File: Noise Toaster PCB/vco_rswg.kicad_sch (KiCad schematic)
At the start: 22 parts, among them Q1 NJFET, U1 LM324, U2 LM324

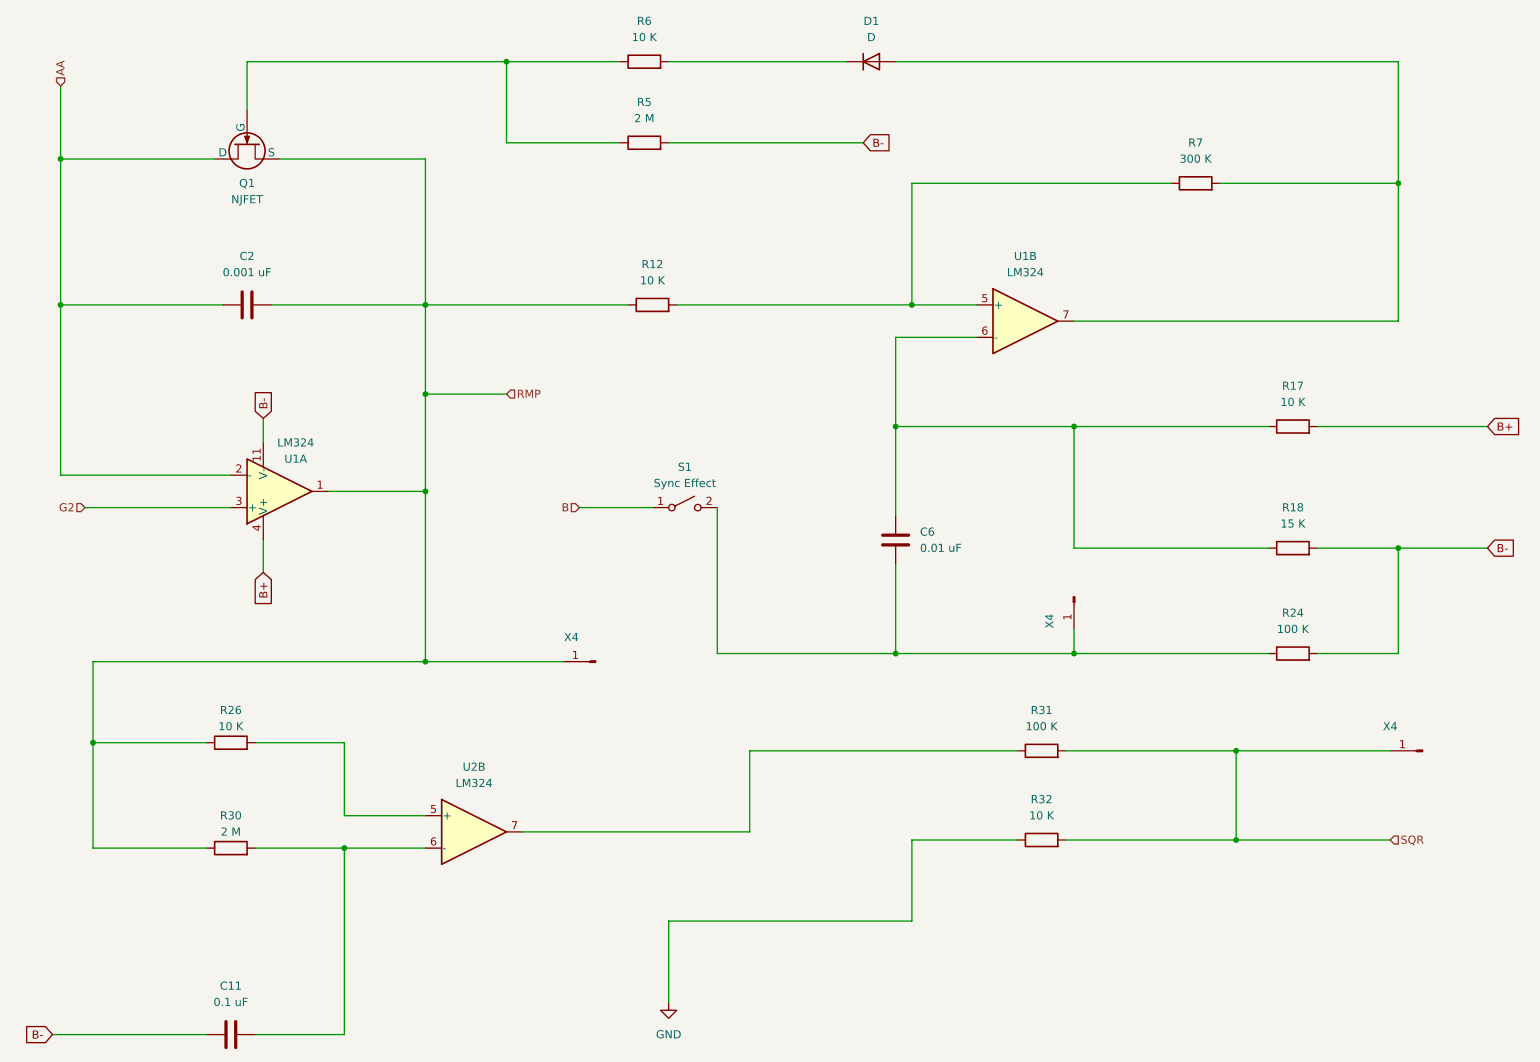
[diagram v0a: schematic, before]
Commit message: updated schematics
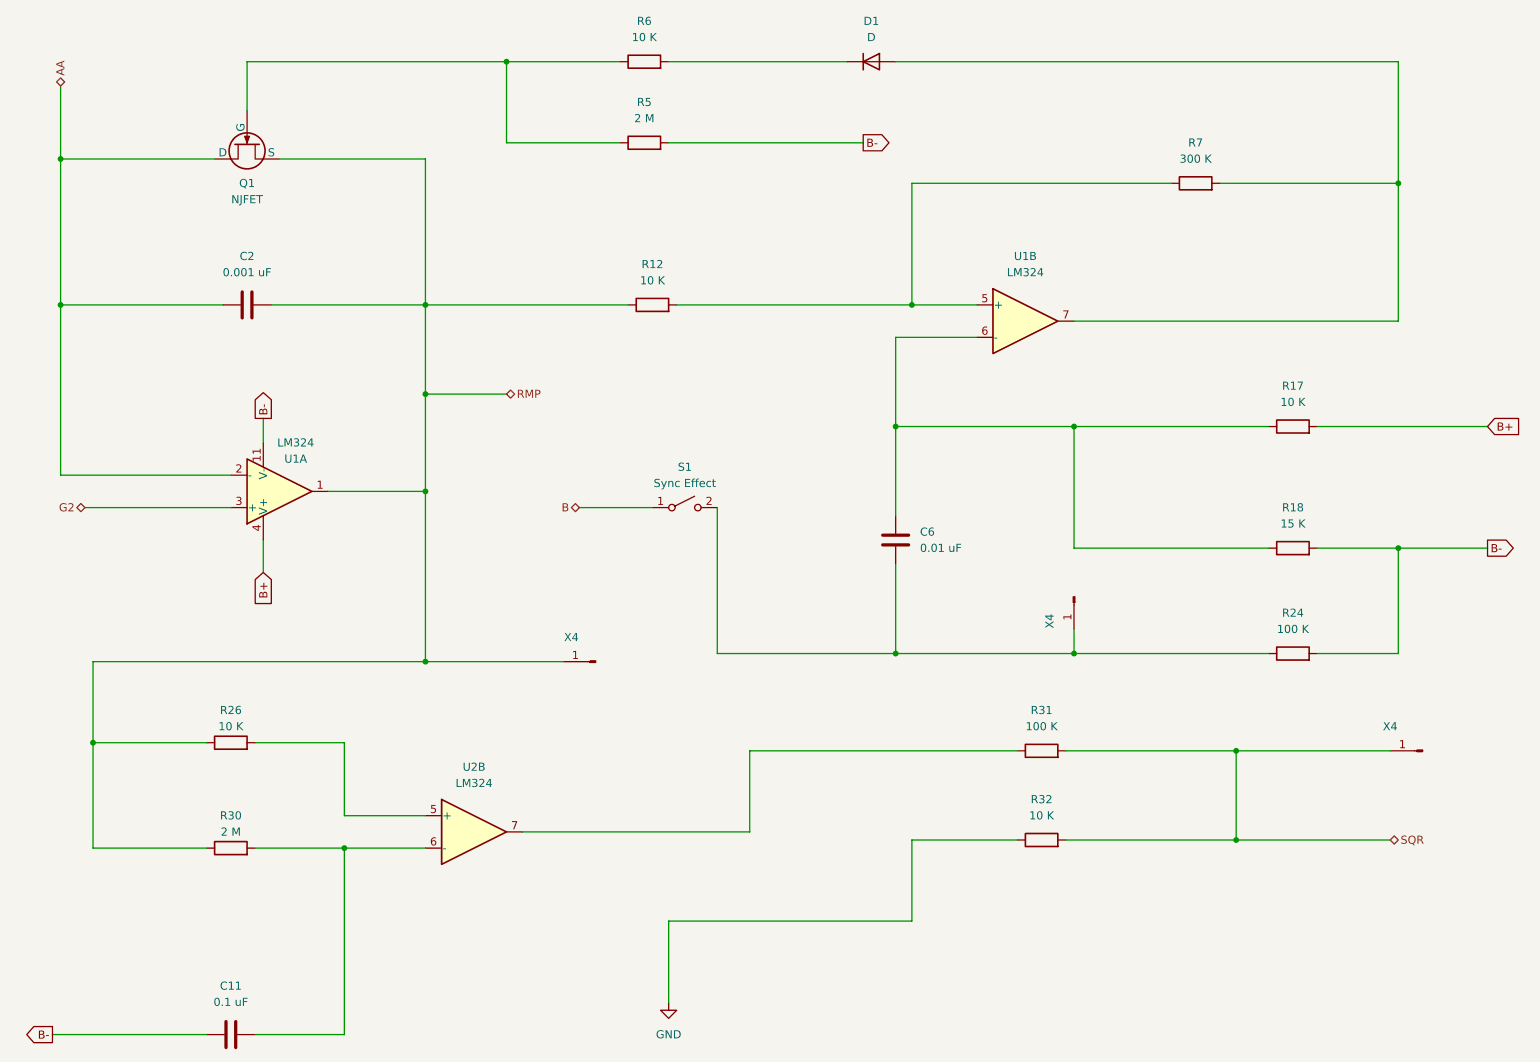
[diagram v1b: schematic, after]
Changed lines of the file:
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@@
     (stroke (width 0) (type default))
   )
-  (global_label "B-" (shape input) (at 157.48 38.1 0) (fields_autoplaced)
+  (global_label "B-" (shape output) (at 157.48 38.1 0) (fields_autoplaced)
     (effects (font (size 1.27 1.27)) (justify left))
     (property "Intersheetrefs" "${INTERSHEET_REFS}" (at 163.3076 38.1 0)
@@
     )
   )
-  (global_label "B-" (shape input) (at 30.48 177.8 180) (fields_autoplaced)
+  (global_label "B-" (shape output) (at 30.48 177.8 180) (fields_autoplaced)
     (effects (font (size 1.27 1.27)) (justify right))
     (property "Intersheetrefs" "${INTERSHEET_REFS}" (at 24.6524 177.8 0)
@@
     )
   )
-  (global_label "B-" (shape input) (at 63.5 81.28 90) (fields_autoplaced)
+  (global_label "B-" (shape output) (at 63.5 81.28 90) (fields_autoplaced)
     (effects (font (size 1.27 1.27)) (justify left))
     (property "Intersheetrefs" "${INTERSHEET_REFS}" (at 63.5 75.4524 90)
@@
     )
   )
-  (global_label "B-" (shape input) (at 255.27 101.6 0) (fields_autoplaced)
+  (global_label "B-" (shape output) (at 255.27 101.6 0) (fields_autoplaced)
     (effects (font (size 1.27 1.27)) (justify left))
     (property "Intersheetrefs" "${INTERSHEET_REFS}" (at 261.0976 101.6 0)
@@
     )
   )
-  (hierarchical_label "G2" (shape input) (at 35.56 95.25 180) (fields_autoplaced)
+  (hierarchical_label "G2" (shape bidirectional) (at 35.56 95.25 180) (fields_autoplaced)
     (effects (font (size 1.27 1.27)) (justify right))
   )
-  (hierarchical_label "B" (shape input) (at 113.03 95.25 180) (fields_autoplaced)
+  (hierarchical_label "B" (shape bidirectional) (at 113.03 95.25 180) (fields_autoplaced)
     (effects (font (size 1.27 1.27)) (justify right))
   )
-  (hierarchical_label "AA" (shape input) (at 31.75 29.21 90) (fields_autoplaced)
-    (effects (font (size 1.27 1.27)) (justify left))
-  )
-  (hierarchical_label "RMP" (shape input) (at 101.6 77.47 0) (fields_autoplaced)
-    (effects (font (size 1.27 1.27)) (justify left))
-  )
-  (hierarchical_label "SQR" (shape input) (at 240.03 147.32 0) (fields_autoplaced)
+  (hierarchical_label "AA" (shape bidirectional) (at 31.75 29.21 90) (fields_autoplaced)
+    (effects (font (size 1.27 1.27)) (justify left))
+  )
+  (hierarchical_label "RMP" (shape bidirectional) (at 101.6 77.47 0) (fields_autoplaced)
+    (effects (font (size 1.27 1.27)) (justify left))
+  )
+  (hierarchical_label "SQR" (shape bidirectional) (at 240.03 147.32 0) (fields_autoplaced)
     (effects (font (size 1.27 1.27)) (justify left))
   )
@@
     (instances
       (project "Noise Toaster PCB"
-        (path "/7be3f398-d902-4566-9ee4-0bff072cd47e/9c6b1f0b-dddb-43c5-83ba-4fcd1cf28662"
-          (reference "#PWR01") (unit 1)
-        )
         (path "/7be3f398-d902-4566-9ee4-0bff072cd47e/a3e9deee-1b9d-4545-a3c9-71b211642b5b"
           (reference "#PWR04") (unit 1)

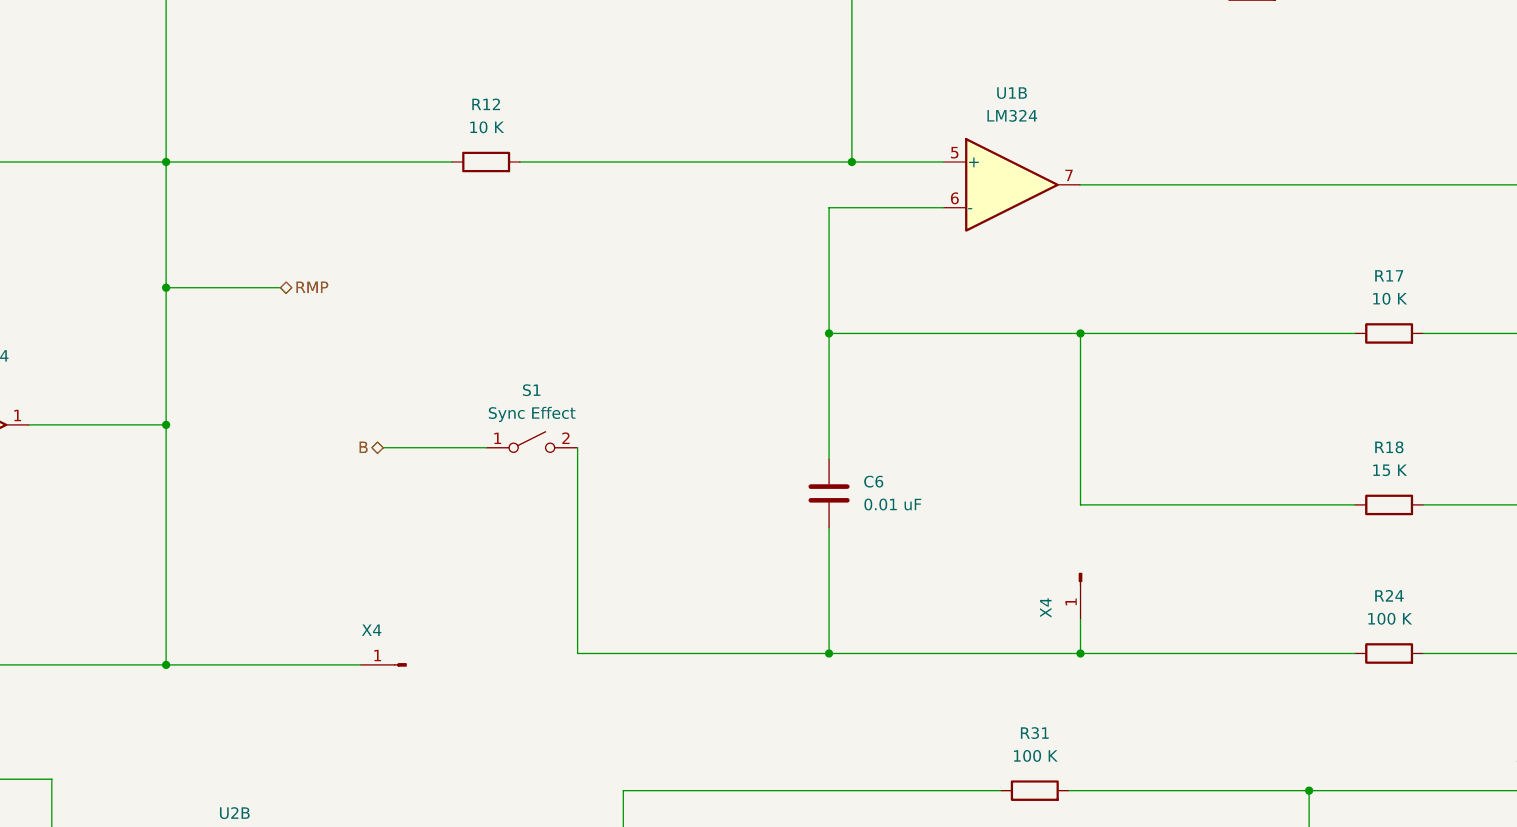
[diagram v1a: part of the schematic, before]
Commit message: refactored the schematic
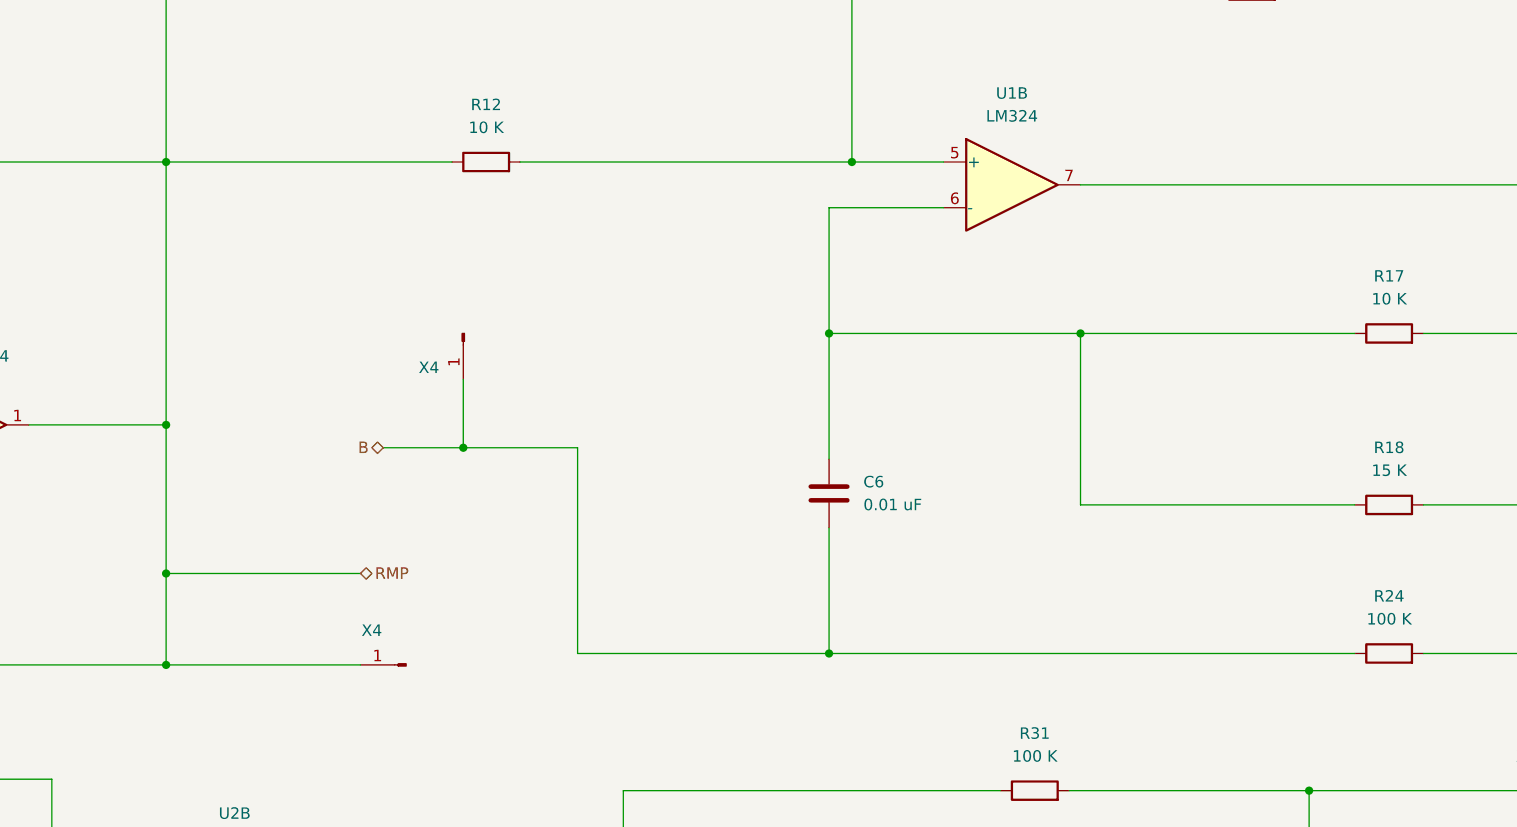
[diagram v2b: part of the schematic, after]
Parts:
- removed S1: Sync Effect, symbol Switch:SW_SPST
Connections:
- net B: now also C6.1, R24.1, X4.1 (Pin_1)
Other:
- moved on the sheet: X4
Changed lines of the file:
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@@
   (junction (at 88.9 119.38) (diameter 0) (color 0 0 0 0)
   )
-  (junction (at 88.9 77.47) (diameter 0) (color 0 0 0 0)
+  (junction (at 121.92 95.25) (diameter 0) (color 0 0 0 0)
   )
   (junction (at 162.56 82.55) (diameter 0) (color 0 0 0 0)
@@
   (junction (at 241.3 44.45) (diameter 0) (color 0 0 0 0)
   )
-  (junction (at 190.5 118.11) (diameter 0) (color 0 0 0 0)
+  (junction (at 88.9 109.22) (diameter 0) (color 0 0 0 0)
   )
   (junction (at 31.75 40.64) (diameter 0) (color 0 0 0 0)
@@
   (junction (at 88.9 63.5) (diameter 0) (color 0 0 0 0)
   )
-  (wire (pts (xy 190.5 118.11) (xy 220.98 118.11))
-    (stroke (width 0) (type default))
-  )
   (wire (pts (xy 31.75 29.21) (xy 31.75 40.64))
     (stroke (width 0) (type default))
@@
     (stroke (width 0) (type default))
   )
+  (wire (pts (xy 88.9 109.22) (xy 88.9 119.38))
+    (stroke (width 0) (type default))
+  )
   (wire (pts (xy 63.5 100.33) (xy 63.5 105.41))
     (stroke (width 0) (type default))
@@
     (stroke (width 0) (type default))
   )
-  (wire (pts (xy 162.56 118.11) (xy 190.5 118.11))
+  (wire (pts (xy 162.56 118.11) (xy 220.98 118.11))
     (stroke (width 0) (type default))
   )
@@
     (stroke (width 0) (type default))
   )
-  (wire (pts (xy 88.9 77.47) (xy 101.6 77.47))
+  (wire (pts (xy 88.9 109.22) (xy 110.49 109.22))
     (stroke (width 0) (type default))
   )
@@
     (stroke (width 0) (type default))
   )
-  (wire (pts (xy 190.5 114.3) (xy 190.5 118.11))
-    (stroke (width 0) (type default))
-  )
   (wire (pts (xy 228.6 101.6) (xy 241.3 101.6))
     (stroke (width 0) (type default))
@@
     (stroke (width 0) (type default))
   )
-  (wire (pts (xy 88.9 63.5) (xy 88.9 77.47))
+  (wire (pts (xy 88.9 63.5) (xy 88.9 92.71))
     (stroke (width 0) (type default))
   )
@@
     (stroke (width 0) (type default))
   )
-  (wire (pts (xy 88.9 77.47) (xy 88.9 92.71))
+  (wire (pts (xy 121.92 87.63) (xy 121.92 95.25))
     (stroke (width 0) (type default))
   )
@@
     (stroke (width 0) (type default))
   )
-  (wire (pts (xy 113.03 95.25) (xy 124.46 95.25))
+  (wire (pts (xy 113.03 95.25) (xy 121.92 95.25))
     (stroke (width 0) (type default))
   )
@@
     (stroke (width 0) (type default))
   )
-  (wire (pts (xy 88.9 92.71) (xy 88.9 119.38))
+  (wire (pts (xy 88.9 92.71) (xy 88.9 109.22))
     (stroke (width 0) (type default))
   )
@@
   )
   (wire (pts (xy 31.75 63.5) (xy 31.75 90.17))
+    (stroke (width 0) (type default))
+  )
+  (wire (pts (xy 121.92 95.25) (xy 134.62 95.25))
     (stroke (width 0) (type default))
   )
@@
     (effects (font (size 1.27 1.27)) (justify right))
   )
-  (hierarchical_label "B" (shape bidirectional) (at 113.03 95.25 180) (fields_autoplaced)
+  (hierarchical_label "B" (shape bidirectional) (at 113.03 95.25 180)
     (effects (font (size 1.27 1.27)) (justify right))
+    (property "Bezeichnung" "X6" (at 111.76 92.71 0)
+      (effects (font (size 1.27 1.27) italic) (justify right))
+    )
   )
   (hierarchical_label "AA" (shape bidirectional) (at 31.75 29.21 90) (fields_autoplaced)
     (effects (font (size 1.27 1.27)) (justify left))
   )
-  (hierarchical_label "RMP" (shape bidirectional) (at 101.6 77.47 0) (fields_autoplaced)
+  (hierarchical_label "RMP" (shape bidirectional) (at 110.49 109.22 0)
     (effects (font (size 1.27 1.27)) (justify left))
-  )
-  (hierarchical_label "SQR" (shape bidirectional) (at 240.03 147.32 0) (fields_autoplaced)
+    (property "Bezeichnung" "X3" (at 110.49 106.68 0)
+      (effects (font (size 1.27 1.27) italic) (justify left))
+    )
+  )
+  (hierarchical_label "SQR" (shape bidirectional) (at 240.03 147.32 0)
     (effects (font (size 1.27 1.27)) (justify left))
+    (property "Bezeichnung" "X7" (at 242.57 149.86 0)
+      (effects (font (size 1.27 1.27) italic) (justify left))
+    )
   )
   (symbol (lib_id "Amplifier_Operational:LM324") (at 96.52 146.05 0) (unit 2)
@@
     )
   )
-  (symbol (lib_id "Switch:SW_SPST") (at 129.54 95.25 0) (unit 1)
-    (in_bom yes) (on_board yes) (dnp no)
-    (property "Reference" "S1" (at 129.54 88.9 0)
-      (effects (font (size 1.27 1.27)))
-    )
-    (property "Value" "Sync Effect" (at 129.54 91.44 0)
-      (effects (font (size 1.27 1.27)))
-    )
-    (property "Footprint" "" (at 129.54 95.25 0)
-      (effects (font (size 1.27 1.27)) hide)
-    )
-    (property "Datasheet" "~" (at 129.54 95.25 0)
-      (effects (font (size 1.27 1.27)) hide)
-    )
-    (pin "1")
-    (pin "2")
-    (instances
-      (project "Noise Toaster PCB"
-        (path "/7be3f398-d902-4566-9ee4-0bff072cd47e/d0369b76-3398-4137-86ba-22490a5aca99"
-          (reference "S1") (unit 1)
-        )
-        (path "/7be3f398-d902-4566-9ee4-0bff072cd47e/a3e9deee-1b9d-4545-a3c9-71b211642b5b"
-          (reference "S2") (unit 1)
-        )
-      )
-    )
-  )
   (symbol (lib_id "Device:R") (at 58.42 148.59 90) (unit 1)
     (in_bom yes) (on_board yes) (dnp no)
@@
     )
   )
-  (symbol (lib_id "Connector:Conn_01x01_Pin") (at 190.5 109.22 270) (unit 1)
+  (symbol (lib_id "Connector:Conn_01x01_Pin") (at 121.92 82.55 270) (unit 1)
     (in_bom yes) (on_board yes) (dnp no)
-    (property "Reference" "X4" (at 186.69 113.03 0)
-      (effects (font (size 1.27 1.27)))
-    )
-    (property "Value" "~" (at 193.04 109.855 0)
-      (effects (font (size 1.27 1.27)))
-    )
-    (property "Footprint" "" (at 190.5 109.22 0)
-      (effects (font (size 1.27 1.27)) hide)
-    )
-    (property "Datasheet" "~" (at 190.5 109.22 0)
+    (property "Reference" "X4" (at 118.11 86.36 90)
+      (effects (font (size 1.27 1.27)))
+    )
+    (property "Value" "~" (at 124.46 83.185 0)
+      (effects (font (size 1.27 1.27)))
+    )
+    (property "Footprint" "" (at 121.92 82.55 0)
+      (effects (font (size 1.27 1.27)) hide)
+    )
+    (property "Datasheet" "~" (at 121.92 82.55 0)
       (effects (font (size 1.27 1.27)) hide)
     )
@@
   (symbol (lib_id "power:GND") (at 127 172.72 0) (unit 1)
     (in_bom yes) (on_board yes) (dnp no)
-    (property "Reference" "#PWR01" (at 127 179.07 0)
-      (effects (font (size 1.27 1.27)) hide)
-    )
+    (property "Reference" "#PWR04" (at 127 179.07 0)
+      (effects (font (size 1.27 1.27)) hide)
+    )
